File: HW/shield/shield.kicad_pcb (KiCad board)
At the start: 2 copper layers, 78 parts, among them J1 TRG, J2 E-STOP, J3 UART, J4 IO, J5 LDP-C BOB, J6 VIN, J7 BREAK, Q1 BSS138, Q2 BSS138, Q3 BSS138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

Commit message: improved guard
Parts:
- moved R40 83.8 mm to (116.0, 87.2)
- moved R39 73.9 mm to (119.8, 87.2)
- moved H2 69.0 mm to (127.6, 75.6)
- moved C1 59.1 mm to (141.4, 105.7), turned to 90 degrees
- moved H1 56.1 mm to (127.6, 92.8)
- moved R37 38.0 mm to (135.0, 83.2), turned to 90 degrees
- moved J7 30.8 mm to (137.9, 86.7), turned to 180 degrees
- moved J5 27.7 mm to (142.9, 114.4), turned to 0 degrees
- moved R36 27.0 mm to (129.3, 88.0), turned to 180 degrees
- moved C9 26.2 mm to (122.7, 82.7)
- moved C7 26.0 mm to (126.2, 80.4)
- moved R34 26.0 mm to (130.0, 80.4)
- moved C10 26.0 mm to (133.0, 81.3)
- moved C8 26.0 mm to (133.0, 85.2)
- moved U2 26.0 mm to (128.0, 84.2)
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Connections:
- net Net-(U2-Pad6) renamed /GUARD
- U2 pad 5: GND -> /GUARDED
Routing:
- net /GUARD: track 0.00 -> 61.8 mm, vias 0 -> 1
- net Net-(C9-Pad2): track 0.00 -> 33.4 mm, vias 0 -> 3
- net GND: track 28.5 -> 0.49 mm, vias 0 -> 3
- net Net-(C7-Pad2): track 0.00 -> 19.2 mm, vias 0 -> 2
- net +5V: track 0.00 -> 15.5 mm
- net /GUARDED: track 8.99 -> 17.4 mm
- net /D_VOUT: track 0.00 -> 5.47 mm
- net Net-(R38-Pad1): track 0.14 -> 2.28 mm
- net Net-(R39-Pad1): track 0.00 -> 1.81 mm
- net Net-(R35-Pad1): track 0.00 -> 1.81 mm
- added copper zone on B.Cu, net GND
- added copper zone on F.Cu, net GND
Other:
- board text added: "! Keep guard clean"
- board text added: "Δ"

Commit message: PCB layout
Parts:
- moved R9 98.2 mm to (135.8, 116.8), turned to -90 degrees
- moved R30 97.0 mm to (148.5, 118.4), turned to -90 degrees
- moved R1 95.0 mm to (138.0, 110.9), turned to -90 degrees
- moved R6 87.6 mm to (153.2, 102.4)
- moved D1 86.7 mm to (176.8, 78.9)
- moved R10 81.4 mm to (172.2, 120.4)
- moved R32 79.3 mm to (151.5, 116.6)
- moved R7 77.7 mm to (158.2, 105.2), turned to 90 degrees
- moved C5 77.4 mm to (139.2, 117.5), turned to 180 degrees
- moved R17 75.8 mm to (162.8, 109.2)
- moved R4 74.2 mm to (140.1, 110.9), turned to 90 degrees
- moved C3 73.5 mm to (161.3, 120.0)
- moved Q6 72.1 mm to (151.5, 119.4), turned to 180 degrees
- moved R5 69.7 mm to (148.5, 105.2)
- moved R8 69.6 mm to (139.2, 114.6), turned to 180 degrees
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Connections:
- A1 pad 13: unconnected-(A1-Pad13) -> /SCL
- A1 pad 14: unconnected-(A1-Pad14) -> /SDA

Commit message: routing
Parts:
- moved D4 23.3 mm to (155.8, 92.3)
- moved D5 23.3 mm to (155.8, 90.2)
- moved D7 23.3 mm to (155.8, 86.1)
- moved R14 23.3 mm to (159.6, 92.3)
- moved R15 23.3 mm to (159.6, 90.2)
- moved R17 23.3 mm to (159.6, 86.1)
- moved D6 23.3 mm to (155.8, 88.1)
- moved R16 23.3 mm to (159.6, 88.1)
- moved R32 10.7 mm to (161.4, 112.5)
- moved Q6 8.69 mm to (159.3, 115.5)
- moved R31 8.69 mm to (162.3, 115.5)
- moved R30 7.93 mm to (156.3, 117.5), turned to 90 degrees
- moved JP1 2.77 mm to (154.2, 110.5), turned to 90 degrees
- moved R4 1.26 mm to (141.0, 110.0), turned to 0 degrees
- moved C3 1.15 mm to (161.1, 118.9)
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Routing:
- added copper zone on F.Cu, net +5V

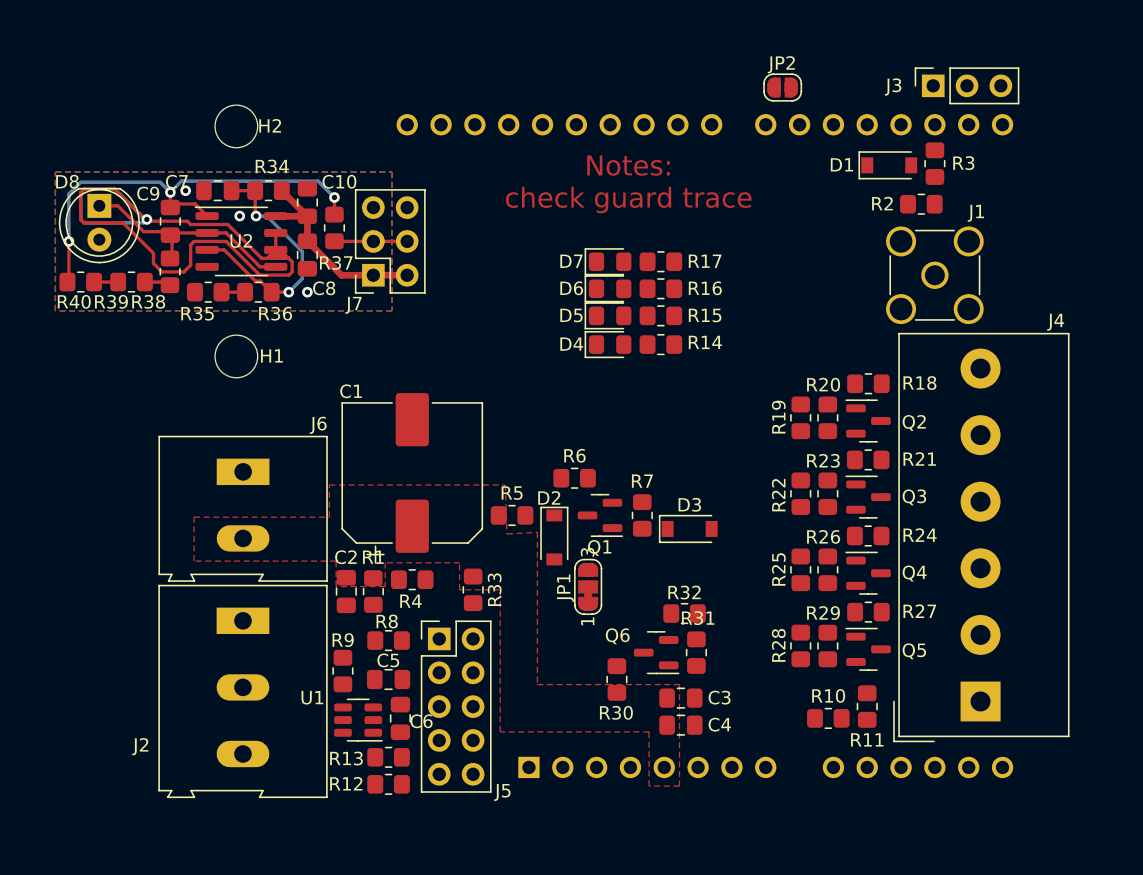
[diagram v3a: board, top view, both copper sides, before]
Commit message: PCB routing finished, needs checking
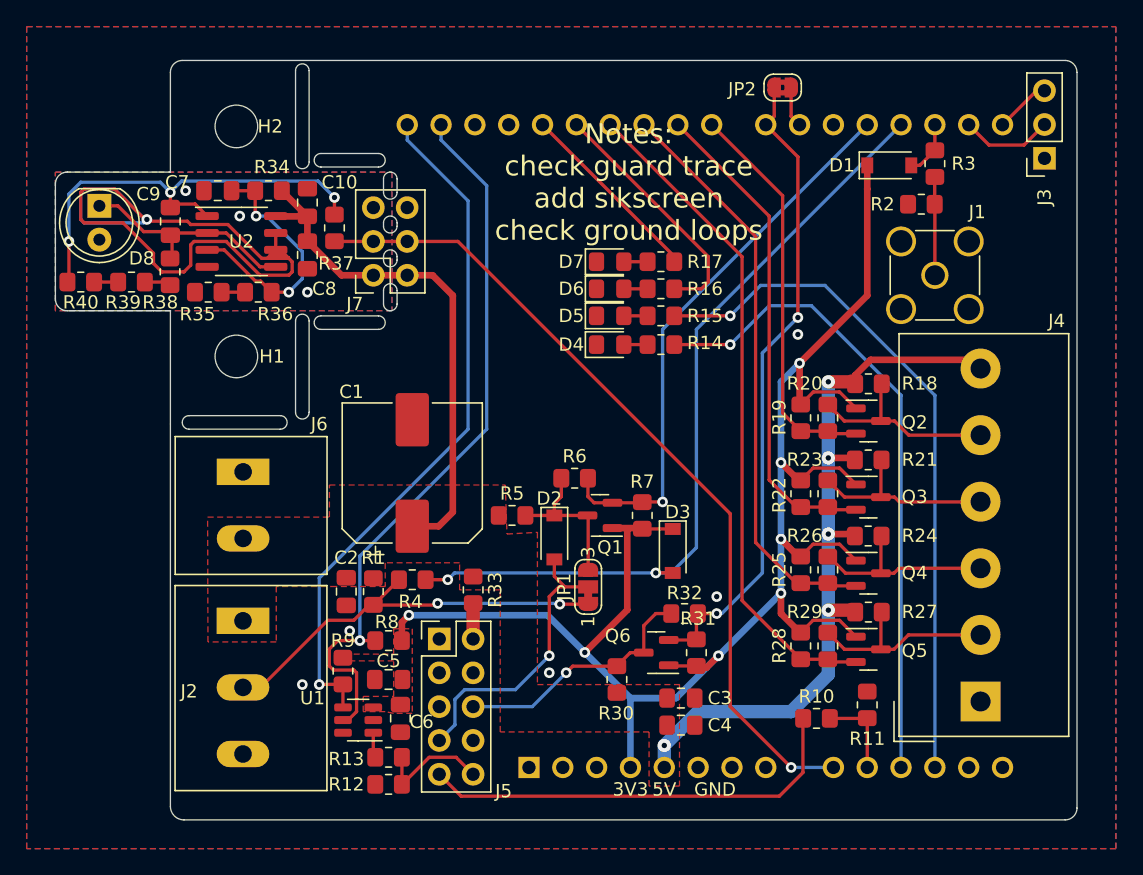
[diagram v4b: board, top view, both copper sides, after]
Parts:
- JP2: footprint Jumper:SolderJumper-2_P1.3mm_Open_RoundedPad1.0x1.5mm -> Jumper:SolderJumper-2_P1.3mm_Bridged2Bar_RoundedPad1.0x1.5mm
- moved J3 9.97 mm to (188.4, 78.3), turned to 180 degrees
- moved D3 2.08 mm to (160.5, 107.8), turned to -90 degrees
- moved R10 0.89 mm to (171.3, 120.4)
- moved R11 0.13 mm to (175.1, 119.4)
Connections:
- A1 pad 11: /LED2 -> /LED1
- A1 pad 12: /LED1 -> /LED2
- A1 pad 13: /SCL -> unconnected-(A1-Pad13)
- A1 pad 14: /SDA -> unconnected-(A1-Pad14)
- J2 pad 1: GND -> +5V
- J2 pad 3: +5V -> GND
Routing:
- net +3V3: track 0.00 -> 128.1 mm, vias 0 -> 7
- net +5V: track 15.5 -> 96.4 mm, vias 0 -> 5
- net /ESTOP: track 0.00 -> 60.7 mm, vias 0 -> 2
- net /D_VOUT: track 5.47 -> 62.3 mm, vias 0 -> 1
- net /SCL: track 0.00 -> 55.5 mm, vias 0 -> 1
- net /SDA: track 0.00 -> 52.1 mm, vias 0 -> 1
- net /LED2: track 0.00 -> 51.9 mm, vias 0 -> 1
- net /IO4: track 0.00 -> 50.3 mm
- net /PULSE: track 0.00 -> 49.0 mm, vias 0 -> 2
- net /LED1: track 0.00 -> 49.0 mm, vias 0 -> 1
- net /IO3: track 0.00 -> 43.7 mm
- net /D_uC_EN: track 0.00 -> 41.9 mm, vias 0 -> 1
- net /IO2: track 0.00 -> 37.0 mm
- net /D_MON: track 0.00 -> 32.8 mm
- net Net-(J2-Pad2): track 0.00 -> 31.3 mm, vias 0 -> 2
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- added copper zone on F.Cu, net +3V3
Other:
- board outline added: 76.7 x 57 mm
- board text added: "3V3"
- board text added: "5V"
- board text added: "GND"
- board text added: "Notes: check guard trace add sikscreen check ground loops"
- board text removed: "Notes: check guard trace"

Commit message: PCB done
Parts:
- moved J6 1.19 mm to (128.3, 103.1)
- moved JP2 0.51 mm to (168.8, 73.5)
- moved C6 0.05 mm to (140.1, 120.4)
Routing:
- net +3V3: track 128.1 -> 131.7 mm
- net GND: track 0.49 -> 3.03 mm, vias 8 -> 135
- net +5V: track 96.4 -> 97.8 mm
- net /GUARD: track 61.8 -> 60.7 mm
- net /PULSE: track 49.0 -> 48.0 mm
- net /SDA: track 52.1 -> 51.2 mm
- net /HV_IO3: track 15.0 -> 15.8 mm
- net /HV_IO4: track 15.3 -> 16.0 mm
- net /D_VOUT: track 62.3 -> 61.6 mm
- net /LED2: track 51.9 -> 51.2 mm
- net /LED1: track 49.0 -> 48.3 mm
- net Net-(C9-Pad2): track 33.4 -> 32.8 mm
- net /IO3: track 43.7 -> 43.2 mm
- net /IO4: track 50.3 -> 49.7 mm
- net /ESTOP: track 60.7 -> 60.2 mm
- added copper zone on B.Cu, net +3V3
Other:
- board text added: "+5V"
- board text added: "A0"
- board text added: "A1"
- board text added: "A2"
- board text added: "A3"
- board text added: "BREAK"
- board text added: "D0"
- board text added: "D1"
- board text added: "D10"
- board text added: "D11"
- board text added: "D12"
- board text added: "D13"
- board text added: "D2"
- board text added: "D3"
- board text added: "D4"
- board text added: "D5"
- board text added: "D6"
- board text added: "D7"
- board text added: "D8"
- board text added: "D9"
- board text added: "E-STOP"
- board text added: "G"
- board text added: "HW SW E-STOP"
- board text added: "IO"
- board text added: "IO1"
- board text added: "IO2"
- board text added: "IO3"
- board text added: "IO4"
- board text added: "LDP-C BOB"
- board text added: "PWM INT"
- board text added: "RX"
- board text added: "SCL"
- board text added: "SDA"
- board text added: "TRIG IN"
- board text added: "TX"
- board text added: "UART"
- board text removed: "Notes: check guard trace add sikscreen check ground loops"

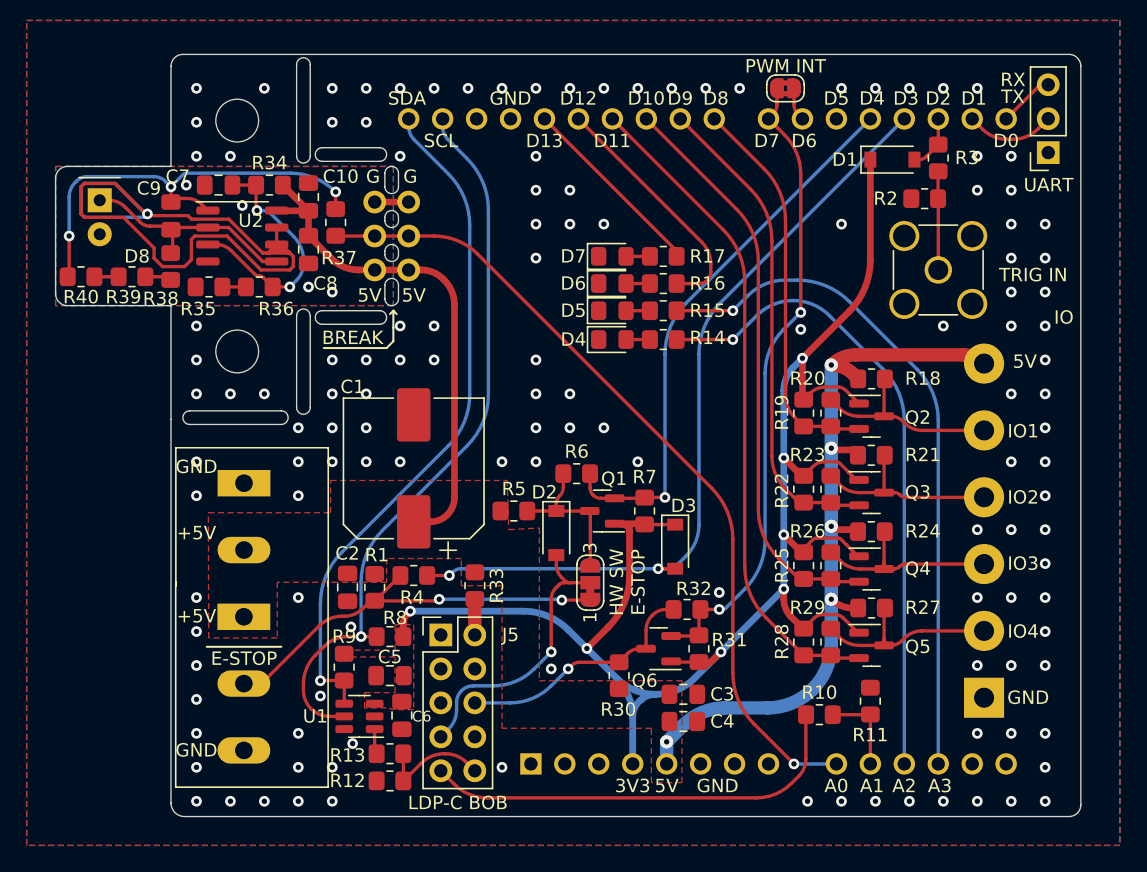
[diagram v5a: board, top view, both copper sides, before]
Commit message: added LDO, BOM
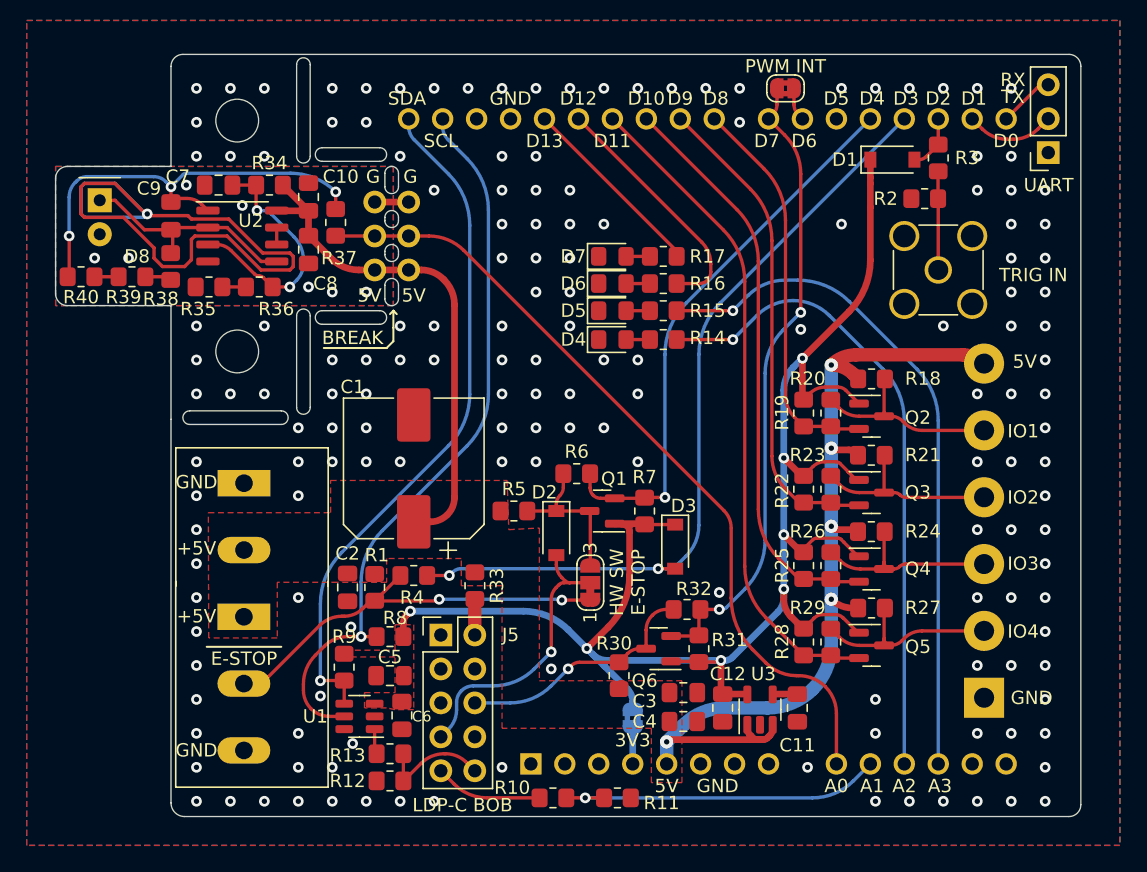
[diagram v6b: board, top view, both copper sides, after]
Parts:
- added C11: 470p, Capacitor_SMD:C_0805_2012Metric_Pad1.18x1.45mm_HandSolder, F.Cu at (169.7, 119.9)
- added C12: 10u, Capacitor_SMD:C_0805_2012Metric_Pad1.18x1.45mm_HandSolder, F.Cu at (164.1, 119.9)
- added JP3: INTR, Jumper:SolderJumper-2_P1.3mm_Bridged2Bar_RoundedPad1.0x1.5mm, B.Cu at (157.4, 120.7)
- added U3: MIC5205-3.3YM5, Package_TO_SOT_SMD:SOT-23-5, F.Cu at (166.9, 120.0)
- moved R10 20.9 mm to (151.4, 126.6)
- moved R11 20.3 mm to (156.2, 126.6), turned to 0 degrees
- moved C3 0.13 mm to (161.1, 118.7)
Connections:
- A1 pad 4: +3V3 -> Net-(A1-Pad4)
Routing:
- net /GUARD: track 60.7 -> 1.13 mm, vias 1 -> 0
- net (no net): track 0.00 -> 55.2 mm, vias 0 -> 1
- net /D_MON: track 32.7 -> 8.06 mm
- net /D_MON_LV: track 6.41 -> 25.0 mm, vias 0 -> 1
- net +5V: track 97.8 -> 108.5 mm
- net Net-(A1-Pad4): track 0.00 -> 2.78 mm
- net Net-(C11-Pad2): track 0.00 -> 1.85 mm
- net /D_VOUT: track 61.6 -> 60.6 mm, vias 1 -> 0
- net +3V3: track 131.7 -> 131.1 mm
- net /HV_IO1: track 15.0 -> 15.5 mm
- net GND: vias 135 -> 169
- removed copper zone on B.Cu, net +3V3
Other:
- board text added: "ALT_LDO"
- board text removed: "IO"
